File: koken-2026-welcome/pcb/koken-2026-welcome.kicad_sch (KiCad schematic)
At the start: 21 parts, among them J1 USB_C_Receptacle_USB2.0_16P, J2 Conn_01x03_Pin, SW1 SW_Push, SW2 SW_SPDT, U1 CH32V003JxMx, U2 AP7333

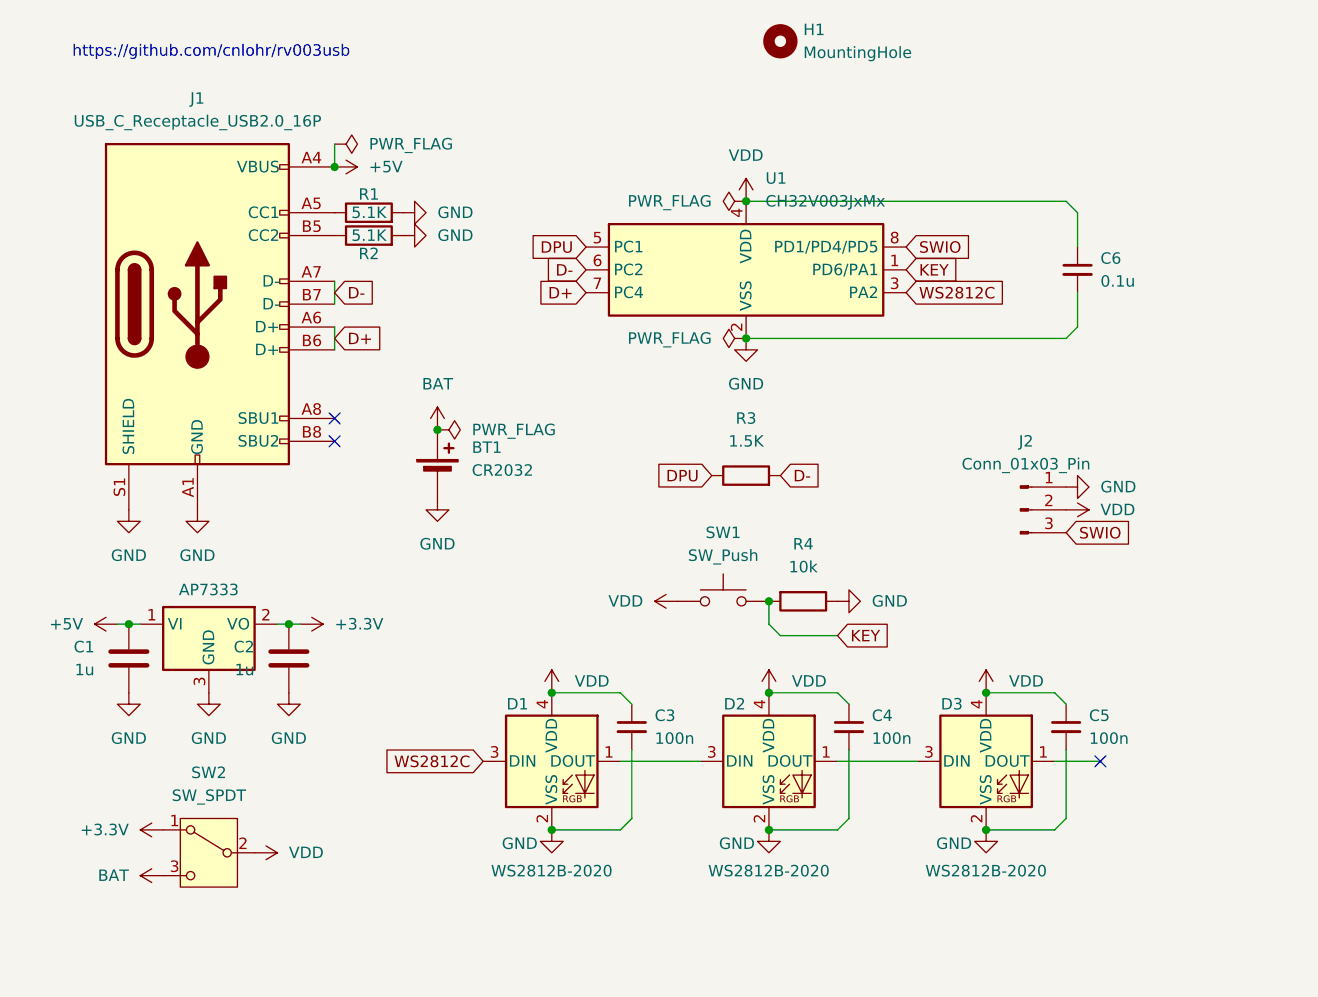
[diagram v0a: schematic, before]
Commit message: koken-2026-welcome 新しい基板の配線を設計
キースイッチをkailhに
ws2812を2個に
ldoを変更
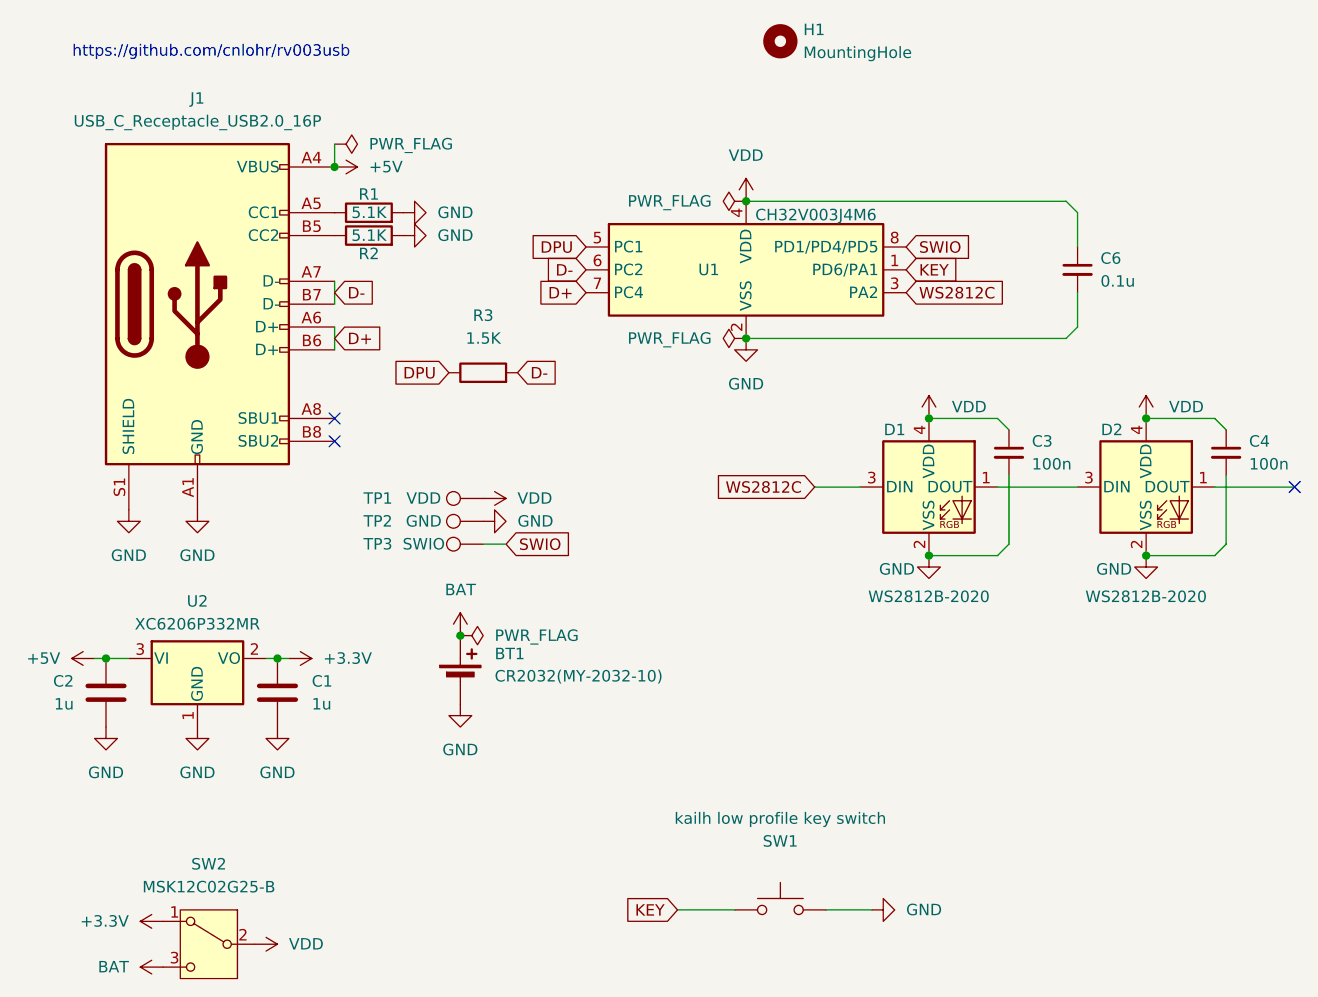
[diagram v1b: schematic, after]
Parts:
- removed C5: 100n, Capacitor_SMD:C_0603_1608Metric_Pad1.08x0.95mm_HandSolder, symbol Device:C_Small
- removed D3: WS2812B-2020, LED_SMD:LED_WS2812B-2020_PLCC4_2.0x2.0mm, symbol LED:WS2812B-2020
- removed J2: Conn_01x03_Pin, Connector_PinHeader_2.54mm:PinHeader_1x03_P2.54mm_Vertical, symbol Connector:Conn_01x03_Pin
- removed R4: 10k, Resistor_SMD:R_0603_1608Metric_Pad0.98x0.95mm_HandSolder, symbol Device:R
- removed U2: AP7333, Library:AP7333, symbol New_Library:AP7333
- added TP1: VDD, TestPoint:TestPoint_Pad_D1.5mm, symbol Connector:TestPoint
- added TP2: GND, TestPoint:TestPoint_Pad_D1.5mm, symbol Connector:TestPoint
- added TP3: SWIO, TestPoint:TestPoint_Pad_D1.5mm, symbol Connector:TestPoint
- added U2: XC6206P332MR, Package_TO_SOT_SMD:SOT-23-3, symbol Regulator_Linear:XC6206PxxxMR
- BT1: value CR2032 -> CR2032(MY-2032-10); footprint Battery:BatteryHolder_Multicomp_BC-2001_1x2032 -> Library:MY-2032-10
- SW1: value SW_Push -> kailh low profile key switch; footprint Library:CherryMX_Red -> Library:SW_Kailh_Choc_V1
- SW2: value SW_SPDT -> MSK12C02G25-B; footprint Button_Switch_THT:SW_Slide-03_Wuerth-WS-SLTV_10x2.5x6.4_P2.54mm -> Library:MSK12C02G25-B
- U1: value CH32V003JxMx -> CH32V003J4M6
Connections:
- net +3.3V: now also C1.1, U2.2 (VO); no longer C2.1
- net +5V: now also C2.1, U2.3 (VI); no longer C1.1
- net GND: now also SW1.2, TP2.1, U2.1 (GND)
- net KEY: now also SW1.1; no longer SW1.2
- net SWIO: now also TP3.1
- net VDD: now also TP1.1; no longer SW1.1
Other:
- moved on the sheet: BT1, C3, C4, D1, D2, R3, SW1, SW2
